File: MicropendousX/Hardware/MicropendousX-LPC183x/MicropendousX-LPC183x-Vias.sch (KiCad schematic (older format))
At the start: 382 parts

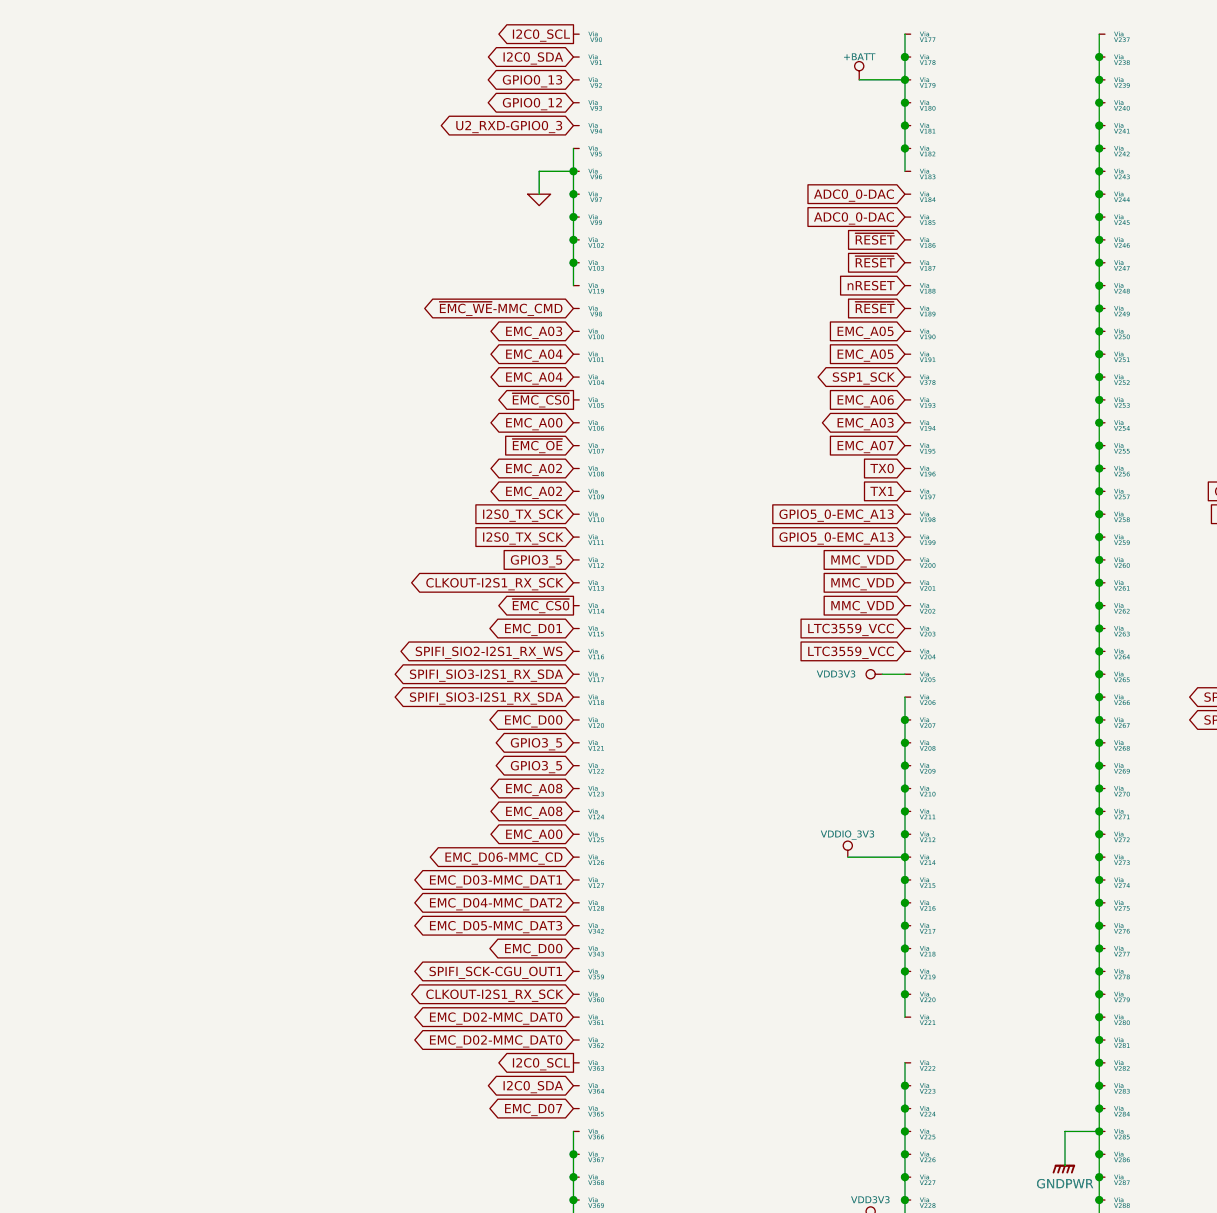
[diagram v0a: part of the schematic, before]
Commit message: Updated MicropendousX-LPC183x portable design with minor post-prototyping corrections.
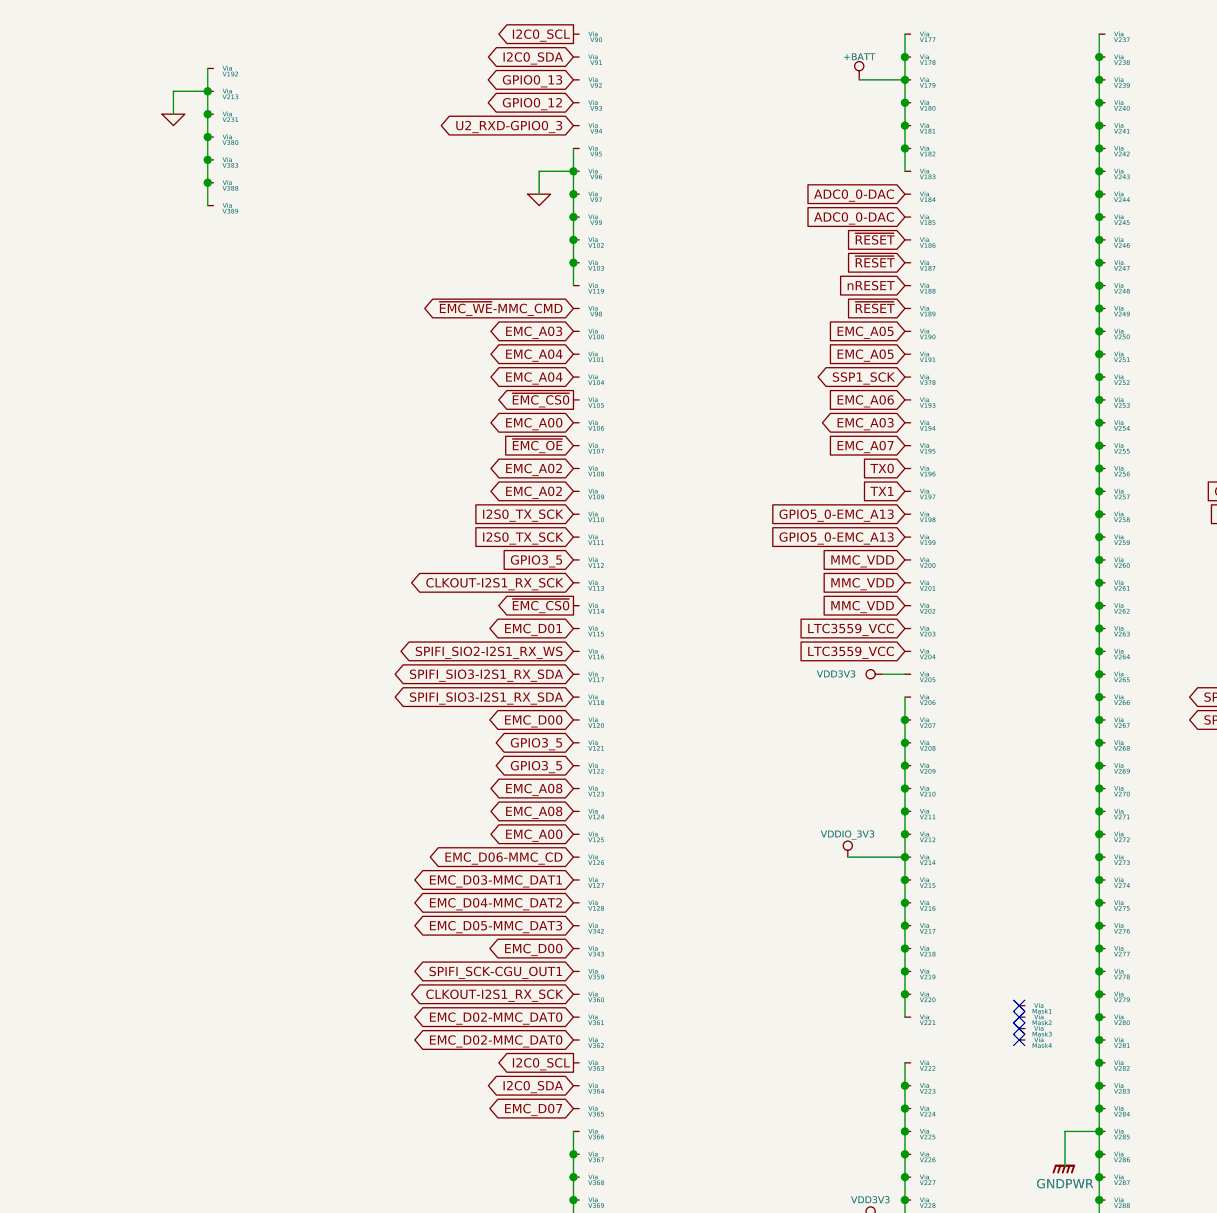
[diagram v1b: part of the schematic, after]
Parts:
- added Mask1, Mask2, Mask3, Mask4: Mask, symbol VIA
- added V192, V213, V231, V380, V383, V388, V389: VIA, symbol VIA
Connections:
- net GND: now also V192.1 (Via), V213.1 (Via), V231.1 (Via), V380.1 (Via), V383.1 (Via), V388.1 (Via), V389.1 (Via)
- no-connect marks 0 -> 4
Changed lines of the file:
@@
-EESchema Schematic File Version 2  date 9/26/2011 2:10:54 AM
+EESchema Schematic File Version 2  date 11/3/2011 5:56:20 AM
 LIBS:power
 LIBS:device
@@
 Sheet 7 7
 Title "MicropendousX-LPC183x"
-Date "26 sep 2011"
+Date "3 nov 2011"
 Rev "1.0"
 Comp "Opendous Inc."
@@
 Comment4 "www.MicropendousX.org"
 $EndDescr
+NoConn ~ 9500 4950
+NoConn ~ 9500 4900
+NoConn ~ 9500 4850
+NoConn ~ 9500 4800
+$Comp
+L VIA Mask3
+U 1 1 4EB27029
+P 9500 4900
+F 0 "Mask3" V 9525 5000 20  0000 C CNN
+F 1 "Mask" H 9500 5100 60  0001 C CNN
+	1    9500 4900
+	0    1    1    0
+$EndComp
+$Comp
+L VIA Mask4
+U 1 1 4EB27028
+P 9500 4950
+F 0 "Mask4" V 9525 5050 20  0000 C CNN
+F 1 "Mask" H 9500 5150 60  0001 C CNN
+	1    9500 4950
+	0    1    1    0
+$EndComp
+$Comp
+L VIA Mask2
+U 1 1 4EB27025
+P 9500 4850
+F 0 "Mask2" V 9525 4950 20  0000 C CNN
+F 1 "Mask" H 9500 5050 60  0001 C CNN
+	1    9500 4850
+	0    1    1    0
+$EndComp
+$Comp
+L VIA Mask1
+U 1 1 4EB26FFE
+P 9500 4800
+F 0 "Mask1" V 9525 4900 20  0000 C CNN
+F 1 "Mask" H 9500 5000 60  0001 C CNN
+	1    9500 4800
+	0    1    1    0
+$EndComp
+$Comp
+L VIA V192
+U 1 1 4EB26FD9
+P 5950 700
+F 0 "V192" V 5975 800 20  0000 C CNN
+F 1 "VIA" H 5950 900 60  0001 C CNN
+	1    5950 700
+	0    1    1    0
+$EndComp
+$Comp
+L VIA V383
+U 1 1 4EB26FD8
+P 5950 1100
+F 0 "V383" V 5975 1200 20  0000 C CNN
+F 1 "VIA" H 5950 1300 60  0001 C CNN
+	1    5950 1100
+	0    1    1    0
+$EndComp
+$Comp
+L VIA V388
+U 1 1 4EB26FD7
+P 5950 1200
+F 0 "V388" V 5975 1300 20  0000 C CNN
+F 1 "VIA" H 5950 1400 60  0001 C CNN
+	1    5950 1200
+	0    1    1    0
+$EndComp
+$Comp
+L VIA V380
+U 1 1 4EB26FD6
+P 5950 1000
+F 0 "V380" V 5975 1100 20  0000 C CNN
+F 1 "VIA" H 5950 1200 60  0001 C CNN
+	1    5950 1000
+	0    1    1    0
+$EndComp
+$Comp
+L VIA V213
+U 1 1 4EB26FD5
+P 5950 800
+F 0 "V213" V 5975 900 20  0000 C CNN
+F 1 "VIA" H 5950 1000 60  0001 C CNN
+	1    5950 800
+	0    1    1    0
+$EndComp
+$Comp
+L VIA V231
+U 1 1 4EB26FD4
+P 5950 900
+F 0 "V231" V 5975 1000 20  0000 C CNN
+F 1 "VIA" H 5950 1100 60  0001 C CNN
+	1    5950 900
+	0    1    1    0
+$EndComp
+$Comp
+L VIA V389
+U 1 1 4EB26FD3
+P 5950 1300
+F 0 "V389" V 5975 1400 20  0000 C CNN
+F 1 "VIA" H 5950 1500 60  0001 C CNN
+	1    5950 1300
+	0    1    1    0
+$EndComp
+$Comp
+L GND #PWR0139
+U 1 1 4EB26FD2
+P 5800 900
+F 0 "#PWR0139" H 5800 900 30  0001 C CNN
+F 1 "GND" H 5800 830 30  0001 C CNN
+	1    5800 900
+	1    0    0    -1
+$EndComp
+Connection ~ 5950 1100
+Connection ~ 5950 800
+Wire Wire Line
+	5800 900  5800 800
+Wire Wire Line
+	5800 800  5950 800
+Connection ~ 5950 900
+Connection ~ 5950 1000
+Wire Wire Line
+	5950 1300 5950 700
+Connection ~ 5950 1200
 Connection ~ 7550 1550
 Wire Wire Line
@@
 $EndComp
 $Comp
-L GND #PWR0139
+L GND #PWR0140
 U 1 1 4E800C5B
 P 10850 950
-F 0 "#PWR0139" H 10850 950 30  0001 C CNN
+F 0 "#PWR0140" H 10850 950 30  0001 C CNN
 F 1 "GND" H 10850 880 30  0001 C CNN
 	1    10850 950
@@
 $EndComp
 $Comp
-L GND #PWR0140
+L GND #PWR0141
 U 1 1 4E800C0C
 P 7400 1250
-F 0 "#PWR0140" H 7400 1250 30  0001 C CNN
+F 0 "#PWR0141" H 7400 1250 30  0001 C CNN
 F 1 "GND" H 7400 1180 30  0001 C CNN
 	1    7400 1250
@@
 GPIO3_5
 $Comp
-L GND #PWR0141
+L GND #PWR0142
 U 1 1 4E7F9AA7
 P 7400 6400
-F 0 "#PWR0141" H 7400 6400 30  0001 C CNN
+F 0 "#PWR0142" H 7400 6400 30  0001 C CNN
 F 1 "GND" H 7400 6330 30  0001 C CNN
 	1    7400 6400
@@
 ~RESET~
 $Comp
-L GNDPWR #PWR0142
+L GNDPWR #PWR0143
 U 1 1 4E7EB475
 P 4500 800
-F 0 "#PWR0142" H 4500 850 40  0001 C CNN
+F 0 "#PWR0143" H 4500 850 40  0001 C CNN
 F 1 "GNDPWR" H 4500 720 40  0000 C CNN
 	1    4500 800
@@
 ~RESET~
 $Comp
-L VDD3V3 #PWR0143
+L VDD3V3 #PWR0144
 U 1 1 4E7EA628
 P 8900 3350
-F 0 "#PWR0143" H 8900 3450 30  0001 C CNN
+F 0 "#PWR0144" H 8900 3450 30  0001 C CNN
 F 1 "VDD3V3" V 8900 3550 30  0000 C CNN
 	1    8900 3350
@@
 ADC0_0-DAC
 $Comp
-L GND #PWR0144
+L GND #PWR0145
 U 1 1 4E7E9B93
 P 10850 6150
-F 0 "#PWR0144" H 10850 6150 30  0001 C CNN
+F 0 "#PWR0145" H 10850 6150 30  0001 C CNN
 F 1 "GND" H 10850 6080 30  0001 C CNN
 	1    10850 6150
@@
 $EndComp
 $Comp
-L 3V3 #PWR0145
+L 3V3 #PWR0146
 U 1 1 4E7E9B5C
 P 10900 5850
-F 0 "#PWR0145" H 10900 5950 40  0001 C CNN
+F 0 "#PWR0146" H 10900 5950 40  0001 C CNN
 F 1 "3V3" V 10900 6000 40  0000 C CNN
 	1    10900 5850
@@
 LTC3559_VCC
 $Comp
-L GND #PWR0146
+L GND #PWR0147
 U 1 1 4E7E51E9
 P 4500 4000
-F 0 "#PWR0146" H 4500 4000 30  0001 C CNN
+F 0 "#PWR0147" H 4500 4000 30  0001 C CNN
 F 1 "GND" H 4500 3930 30  0001 C CNN
 	1    4500 4000
@@
 TMS
 $Comp
-L VBUS #PWR0147
+L VBUS #PWR0148
 U 1 1 4E771EB8
 P 10950 1350
-F 0 "#PWR0147" H 10950 1450 30  0001 C CNN
+F 0 "#PWR0148" H 10950 1450 30  0001 C CNN
 F 1 "VBUS" V 10950 1500 30  0000 C CNN
 	1    10950 1350
@@
 I2C1_SCL-U3_RXD
 $Comp
-L GND #PWR0148
+L GND #PWR0149
 U 1 1 4E76CD8A
 P 2300 5250
-F 0 "#PWR0148" H 2300 5250 30  0001 C CNN
+F 0 "#PWR0149" H 2300 5250 30  0001 C CNN
 F 1 "GND" H 2300 5180 30  0001 C CNN
 	1    2300 5250
@@
 $EndComp
 $Comp
-L GND #PWR0149
+L GND #PWR0150
 U 1 1 4E76CCD0
 P 2300 6850
-F 0 "#PWR0149" H 2300 6850 30  0001 C CNN
+F 0 "#PWR0150" H 2300 6850 30  0001 C CNN
 F 1 "GND" H 2300 6780 30  0001 C CNN
 	1    2300 6850
@@
 $EndComp
 $Comp
-L +BATT #PWR0150
+L +BATT #PWR0151
 U 1 1 4E76C805
 P 8800 750
-F 0 "#PWR0150" H 8800 700 20  0001 C CNN
+F 0 "#PWR0151" H 8800 700 20  0001 C CNN
 F 1 "+BATT" H 8800 850 30  0000 C CNN
 	1    8800 750
@@
 SSP1_SSEL
 $Comp
-L GND #PWR0151
+L GND #PWR0152
 U 1 1 4E74194B
 P 10850 4800
-F 0 "#PWR0151" H 10850 4800 30  0001 C CNN
+F 0 "#PWR0152" H 10850 4800 30  0001 C CNN
 F 1 "GND" H 10850 4730 30  0001 C CNN
 	1    10850 4800
@@
 USB0_DM
 $Comp
-L VDDIO_3V3 #PWR0152
+L VDDIO_3V3 #PWR0153
 U 1 1 4E49585F
 P 8750 4150
-F 0 "#PWR0152" H 8750 4250 30  0001 C CNN
+F 0 "#PWR0153" H 8750 4250 30  0001 C CNN
 F 1 "VDDIO_3V3" H 8750 4250 30  0000 C CNN
 	1    8750 4150
@@
 $EndComp
 $Comp
-L VDD3V3 #PWR0153
+L VDD3V3 #PWR0154
 U 1 1 4E49554D
 P 8850 5750
-F 0 "#PWR0153" H 8850 5850 30  0001 C CNN
+F 0 "#PWR0154" H 8850 5850 30  0001 C CNN
 F 1 "VDD3V3" H 8850 5850 30  0000 C CNN
 	1    8850 5750
@@
 $EndComp
 $Comp
-L GNDPWR #PWR0154
+L GNDPWR #PWR0155
 U 1 1 4E24500E
 P 9700 5500
-F 0 "#PWR0154" H 9700 5550 40  0001 C CNN
+F 0 "#PWR0155" H 9700 5550 40  0001 C CNN
 F 1 "GNDPWR" H 9700 5420 40  0000 C CNN
 	1    9700 5500
@@
 $EndComp
 $Comp
-L 5V0 #PWR0155
+L 5V0 #PWR0156
 U 1 1 4E244116
 P 10900 6450
-F 0 "#PWR0155" H 10900 6550 30  0001 C CNN
+F 0 "#PWR0156" H 10900 6550 30  0001 C CNN
 F 1 "5V0" V 10900 6600 30  0000 C CNN
 	1    10900 6450
@@
 $EndComp
 $Comp
-L VDDIO_3V3 #PWR0156
+L VDDIO_3V3 #PWR0157
 U 1 1 4E2437D2
 P 2200 3900
-F 0 "#PWR0156" H 2200 4000 30  0001 C CNN
+F 0 "#PWR0157" H 2200 4000 30  0001 C CNN
 F 1 "VDDIO_3V3" H 2200 4000 30  0000 C CNN
 	1    2200 3900
@@
 $EndComp
 $Comp
-L GND #PWR0157
+L GND #PWR0158
 U 1 1 4E24344B
 P 4500 5000
-F 0 "#PWR0157" H 4500 5000 30  0001 C CNN
+F 0 "#PWR0158" H 4500 5000 30  0001 C CNN
 F 1 "GND" H 4500 4930 30  0001 C CNN
 	1    4500 5000
@@
 $EndComp
 $Comp
-L VBUS #PWR0158
+L VBUS #PWR0159
 U 1 1 4E2423A0
 P 2200 6500
-F 0 "#PWR0158" H 2200 6600 30  0001 C CNN
+F 0 "#PWR0159" H 2200 6600 30  0001 C CNN
 F 1 "VBUS" H 2200 6600 30  0000 C CNN
 	1    2200 6500
@@
 $EndComp
 $Comp
-L GND #PWR0159
+L GND #PWR0160
 U 1 1 4E241B4C
 P 2300 1450
-F 0 "#PWR0159" H 2300 1450 30  0001 C CNN
+F 0 "#PWR0160" H 2300 1450 30  0001 C CNN
 F 1 "GND" H 2300 1380 30  0001 C CNN
 	1    2300 1450
